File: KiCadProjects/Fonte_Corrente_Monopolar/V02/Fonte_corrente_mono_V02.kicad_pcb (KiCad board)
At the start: 2 copper layers, 90 x 100 mm, 23 parts, among them J1 Vref, J2 tensoes, J3 sinais analogicos, J4 comunicacao / sinais digitais, U1-howland1 AD828AN, U2 INA128, U3-cond1 AD828AN

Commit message: baseado barramento v04
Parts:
- removed SW_kcd1: sw, Chave_Gangorra:chave gangorra 3 pinos
- removed U1-howland1: AD828AN, AD828AN:N_8_ADI
- added J7: Vref, Connector_PinHeader_2.54mm:PinHeader_1x03_P2.54mm_Vertical, F.Cu at (143.6, 42.8)
- added U1: AD828AN, AD828:AD828, F.Cu at (116.2, 118.3)
- J1: value Vref -> alimentacao analogica; footprint Connector_PinHeader_2.54mm:PinHeader_1x03_P2.54mm_Vertical -> Connector_PinHeader_2.54mm:PinHeader_1x08_P2.54mm_Vertical
- J2: value tensoes -> sinais analogicos; footprint Connector_PinSocket_2.54mm:PinSocket_1x08_P2.54mm_Vertical -> Connector_PinHeader_2.54mm:PinHeader_1x27_P2.54mm_Vertical
- J3: value sinais analogicos -> comunicacao / sinais digitais; footprint Connector_PinSocket_2.54mm:PinSocket_1x27_P2.54mm_Vertical -> Connector_PinHeader_2.54mm:PinHeader_1x35_P2.54mm_Vertical
- J4: value comunicacao / sinais digitais -> Change_signal; footprint Connector_PinSocket_2.54mm:PinSocket_1x35_P2.54mm_Vertical -> Connector_PinHeader_2.54mm:PinHeader_1x03_P2.54mm_Vertical
- U2: value INA128 -> INA128-H1
- U3-cond1: footprint AD828AN:N_8_ADI -> AD828:AD828
- moved J4 106.2 mm to (113.7, 134.3), turned to 90 degrees
- moved C4 90.2 mm to (164.7, 44.8)
- moved J3 87.0 mm to (185.8, 45.0)
- moved J1 83.4 mm to (107.1, 45.0), turned to 0 degrees
- moved R11 72.1 mm to (165.1, 57.7), turned to 0 degrees
- moved R12 69.9 mm to (160.4, 57.4), turned to 90 degrees
- moved D2 69.3 mm to (167.6, 71.4)
- moved R10 64.5 mm to (176.1, 51.7), turned to 180 degrees
- moved D1 58.4 mm to (177.9, 64.3)
- moved U3-cond1 56.9 mm to (145.1, 54.7)
- moved C3 48.5 mm to (159.2, 65.5), turned to 0 degrees
- moved R6 44.0 mm to (144.1, 113.5)
- moved R5 41.7 mm to (133.8, 128.6), turned to 0 degrees
- moved R3 35.3 mm to (131.1, 121.9)
- moved U2 34.5 mm to (118.9, 89.2)
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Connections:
- J1 pad 1: +3.3V -> VCC
- J1 pad 2: Net-(D1-K) -> VEE
- J1 pad 3: +5V -> Earth
- J2 pad 1: Earth -> unconnected-(J2-Pin_1-Pad1)
- J2 pad 2: VCC -> unconnected-(J2-Pin_2-Pad2)
- J2 pad 3: VEE -> unconnected-(J2-Pin_3-Pad3)
- J2 pad 4: +9V -> unconnected-(J2-Pin_4-Pad4)
- J2 pad 5: -9V -> unconnected-(J2-Pin_5-Pad5)
- J2 pad 6: +5V -> unconnected-(J2-Pin_6-Pad6)
- J2 pad 7: -5V -> unconnected-(J2-Pin_7-Pad7)
- J2 pad 8: +3.3V -> unconnected-(J2-Pin_8-Pad8)
- J3 pad 1: unconnected-(J3-Pin_1-Pad1) -> +5V
- J3 pad 16: unconnected-(J3-Pin_16-Pad16) -> Earth
- J3 pad 17: unconnected-(J3-Pin_17-Pad17) -> CS1
- J3 pad 18: unconnected-(J3-Pin_18-Pad18) -> CS0
- J3 pad 19: unconnected-(J3-Pin_19-Pad19) -> SPI_clk
- J3 pad 2: unconnected-(J3-Pin_2-Pad2) -> -5V
- J3 pad 20: I1 -> SPI_CIPO
- J3 pad 21: I2 -> SPI_COPI
- J3 pad 22: Ampl1 -> Earth
- J3 pad 23: Ampl2 -> SCL4
- J3 pad 24: Sin1 -> SDA4
- J3 pad 25: Sin2 -> Earth
- J3 pad 26: SinA -> SCL3
- J3 pad 27: SinB -> SDA3
- J3 pad 3: unconnected-(J3-Pin_3-Pad3) -> Earth
- J3 pad 4: unconnected-(J3-Pin_4-Pad4) -> Earth
- J3 pad 5: unconnected-(J3-Pin_5-Pad5) -> +3.3V
- J3 pad 6: unconnected-(J3-Pin_6-Pad6) -> Earth
- J3 pad 7: unconnected-(J3-Pin_7-Pad7) -> Earth
- J4 pad 1: SINC -> SinA
- J4 pad 2: SPI_COPI -> Net-(J4-Pin_2)
- J4 pad 3: SPI_CIPO -> Sin1
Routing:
- net Earth: track 244.0 -> 0.00 mm
- net +3.3V: track 162.9 -> 0.00 mm, vias 2 -> 0
- net +9V: track 151.1 -> 0.00 mm, vias 4 -> 0
- net Net-(U1-howland1-+IN1): track 136.8 -> 0.00 mm
- net -9V: track 126.9 -> 0.00 mm, vias 2 -> 0
- net +5V: track 123.7 -> 0.00 mm
- net out_corrente: track 102.9 -> 0.00 mm, vias 2 -> 0
- net Ampl1: track 74.5 -> 0.00 mm
- net Net-(D1-K): track 63.0 -> 0.00 mm
- net Net-(U1-howland1-+IN2): track 45.4 -> 0.00 mm
- net nó2: track 40.9 -> 0.00 mm
- net SinA: track 31.8 -> 0.00 mm, vias 2 -> 0
- net V_INA: track 24.4 -> 0.00 mm
- net out_buffer: track 23.5 -> 0.00 mm
- net Net-(U1-howland1-OUT2): track 22.5 -> 0.00 mm
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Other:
- board text added: "+3.3V"
- board text added: "+5V"
- board text added: "+9V"
- board text added: "-5V"
- board text added: "-9V"
- board text added: "AGND"
- board text added: "Ampl1"
- board text added: "Ampl2"
- board text added: "CS0"
- board text added: "CS1"
- board text added: "Fonte corrente monopolar V02 2024"
- board text added: "GND"
- board text added: "I1"
- board text added: "I2"
- board text added: "SCL1"
- board text added: "SCL2"
- board text added: "SCL3"
- board text added: "SCL4"
- board text added: "SDA1"
- board text added: "SDA2"
- board text added: "SDA3"
- board text added: "SDA4"
- board text added: "SINCD"
- board text added: "SPI_CIPO"
- board text added: "SPI_COPI"
- board text added: "SPI_clk"
- board text added: "Sin1"
- board text added: "Sin2"
- board text added: "SinA"
- board text added: "SinB"
- board text added: "VCC"
- board text added: "VEE"
- board text removed: "+3.3V | +5.0V"
- board text removed: "Fonte de corrente monopolar Howland aperfeiçoada v01 - 2023"

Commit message: Baseado barramento v04 - Finalizado
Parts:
- SinA | Sin1: renamed from J4
- moved D2 0.38 mm to (167.5, 71.1)
- moved R10 0.38 mm to (176.0, 51.4)
- moved R11 0.38 mm to (164.9, 57.4)
- moved R3 0.38 mm to (130.9, 121.6)
- moved J2 0.38 mm to (106.9, 68.8)
- moved R1 0.38 mm to (126.4, 106.6)
- moved RganhoINA1 0.38 mm to (121.8, 82.6)
- moved SinA | Sin1 0.38 mm to (113.5, 134.0)
- moved U1 0.38 mm to (116.0, 117.9)
- moved U2 0.38 mm to (118.8, 88.9)
- moved R12 0.38 mm to (160.3, 57.1)
- moved U3 0.38 mm to (144.9, 54.3)
- moved R4 0.38 mm to (138.5, 110.0)
- moved R5 0.38 mm to (133.6, 128.3)
- moved J1 0.38 mm to (106.9, 44.7)
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- renumbered U3-cond1 to U3, J7 to Vref
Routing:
- net Earth: track 0.00 -> 335.7 mm
- net +9V: track 0.00 -> 113.2 mm
- net Ampl1: track 0.00 -> 112.7 mm
- net -9V: track 0.00 -> 105.4 mm
- net out_corrente: track 0.00 -> 87.0 mm
- net +3.3V: track 0.00 -> 49.4 mm
- net Net-(D1-K): track 0.00 -> 49.2 mm
- net V_INA: track 0.00 -> 44.0 mm
- net +5V: track 0.00 -> 41.0 mm
- net Net-(U1-howland1-OUT2): track 0.00 -> 23.6 mm
- net Sin1: track 0.00 -> 23.2 mm
- net Net-(U1-howland1--IN2): track 0.00 -> 23.0 mm
- net nó2: track 0.00 -> 20.8 mm
- net I1: track 0.00 -> 18.2 mm
- net Net-(U1-howland1-+IN2): track 0.00 -> 15.1 mm
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- added copper zone on B.Cu, net Earth
- added copper zone on F.Cu, net Earth
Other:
- board text added: "+3.3V | +5.0V"
- board text added: "signal select"

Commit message: Baseado barramento v04 - Finalizado
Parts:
- removed SinA | Sin1: Change_signal, Connector_PinHeader_2.54mm:PinHeader_1x03_P2.54mm_Vertical
- removed U1, U3: AD828AN, AD828:AD828
- removed Vref: Vref, Connector_PinHeader_2.54mm:PinHeader_1x03_P2.54mm_Vertical
- added D3: LED - Red, LED_THT:LED_D5.0mm, F.Cu at (128.0, 44.0)
- added D4: LED - Green, LED_THT:LED_D5.0mm, F.Cu at (121.0, 44.0)
- added D5: LED - Yelow, LED_THT:LED_D5.0mm, F.Cu at (114.0, 44.0)
- added D6: LED - Blue, LED_THT:LED_D5.0mm, F.Cu at (135.0, 44.0)
- added J4: signal select, Connector_PinHeader_2.54mm:PinHeader_1x03_P2.54mm_Vertical, F.Cu at (113.7, 134.0)
- added J7: Vref, Connector_PinHeader_2.54mm:PinHeader_1x03_P2.54mm_Vertical, F.Cu at (149.5, 42.6)
- added R13: 390, Resistor_THT:R_Axial_DIN0207_L6.3mm_D2.5mm_P7.62mm_Horizontal, F.Cu at (122.7, 60.7)
- added R7: 360, Resistor_THT:R_Axial_DIN0207_L6.3mm_D2.5mm_P7.62mm_Horizontal, F.Cu at (119.5, 55.2)
- added R8: 160, Resistor_THT:R_Axial_DIN0207_L6.3mm_D2.5mm_P7.62mm_Horizontal, F.Cu at (143.8, 56.3)
- added R9: 82, Resistor_THT:R_Axial_DIN0207_L6.3mm_D2.5mm_P7.62mm_Horizontal, F.Cu at (136.4, 51.8)
- added U1-howland1: AD828AN, AD828:AD828, F.Cu at (118.7, 113.9)
- added U3-cond1: AD828AN, AD828:AD828, F.Cu at (147.8, 60.1)
- U2: value INA128-H1 -> INA128
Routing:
- net Earth: track 335.7 -> 380.3 mm
- net nó2: track 20.8 -> 50.0 mm
- net Net-(D6-A): track 0.00 -> 19.7 mm
- net out_corrente: track 87.0 -> 67.5 mm
- net Net-(D4-A): track 0.00 -> 18.3 mm
- net Net-(D5-A): track 0.00 -> 15.5 mm
- net +5V: track 41.0 -> 54.3 mm
- net Net-(D3-K): track 0.00 -> 13.0 mm
- net +3.3V: track 49.4 -> 58.9 mm
- net nó1: track 13.5 -> 6.14 mm
- net -9V: track 105.4 -> 112.6 mm
- net Ampl1: track 112.7 -> 107.2 mm
- net out_buffer: track 15.0 -> 9.91 mm
- net Net-(U1-howland1-OUT2): track 23.6 -> 19.0 mm
- net Net-(D1-K): track 49.2 -> 45.0 mm
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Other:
- board text removed: "+3.3V | +5.0V"
- board text removed: "signal select"

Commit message: Baseado barramento v04 - Finalizado - mudanca valor resitor leds
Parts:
- R13: value 390 -> 1.2k
- R7: value 360 -> 1.2k
- R8: value 160 -> 390
- R9: value 82 -> 240
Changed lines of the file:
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@@
         (effects (font (size 1 1) (thickness 0.15)))
     )
-    (fp_text value "82" (at 3.81 2.37) (layer "F.Fab")
+    (fp_text value "240" (at 3.81 2.37) (layer "F.Fab")
         (effects (font (size 1 1) (thickness 0.15)))
     )
@@
         (effects (font (size 1 1) (thickness 0.15)))
     )
-    (fp_text value "160" (at 3.81 2.37) (layer "F.Fab")
+    (fp_text value "390" (at 3.81 2.37) (layer "F.Fab")
         (effects (font (size 1 1) (thickness 0.15)))
     )
@@
         (effects (font (size 1 1) (thickness 0.15)))
     )
-    (fp_text value "360" (at 3.81 2.37) (layer "F.Fab")
+    (fp_text value "1.2k" (at 3.81 2.37) (layer "F.Fab")
         (effects (font (size 1 1) (thickness 0.15)))
     )
@@
         (effects (font (size 1 1) (thickness 0.15)))
     )
-    (fp_text value "390" (at 3.81 2.37) (layer "F.Fab")
-        (effects (font (size 1 1) (thickness 0.15)))
-    )
+    (fp_text value "1.2k" (at 3.81 2.37) (layer "F.Fab")
+        (effects (font (size 1 1) (thickness 0.15)))
+    )

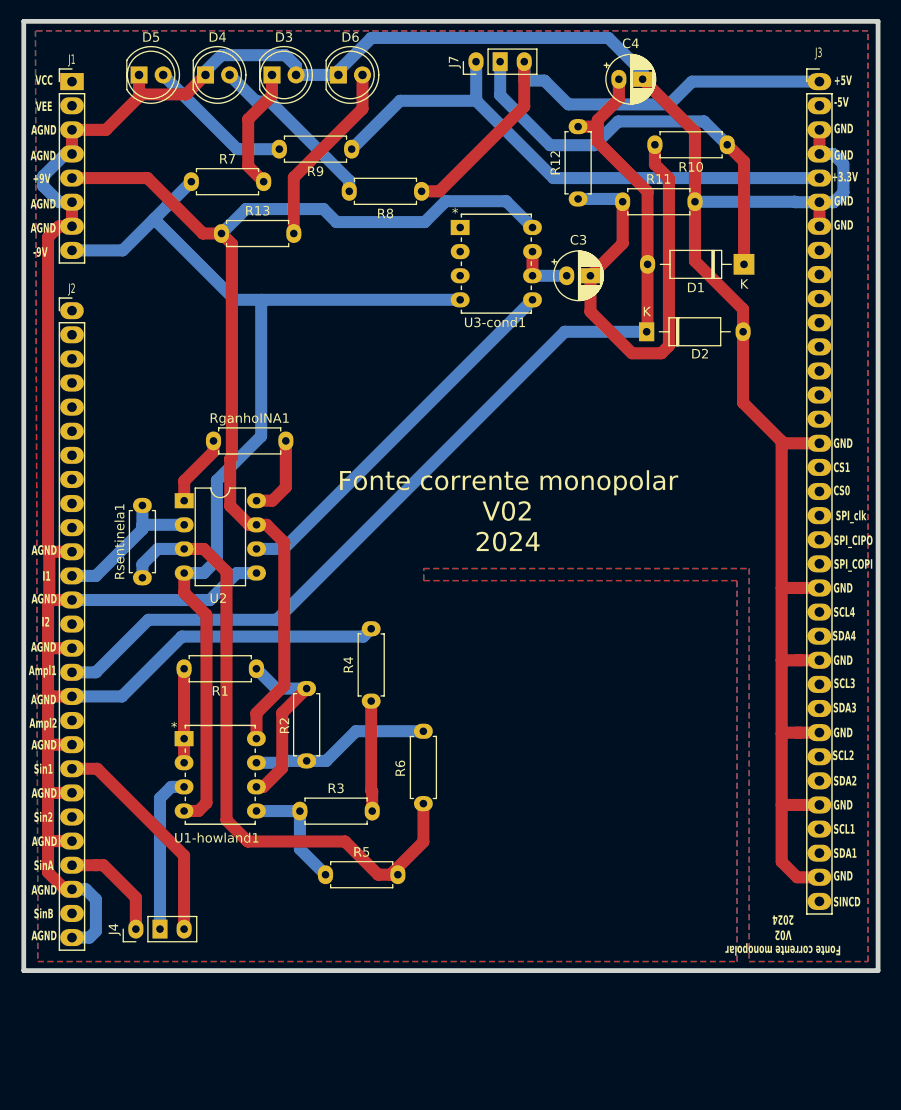
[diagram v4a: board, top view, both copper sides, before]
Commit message: Baseado barramento v04 - Finalizado - mudanca valor resitor leds
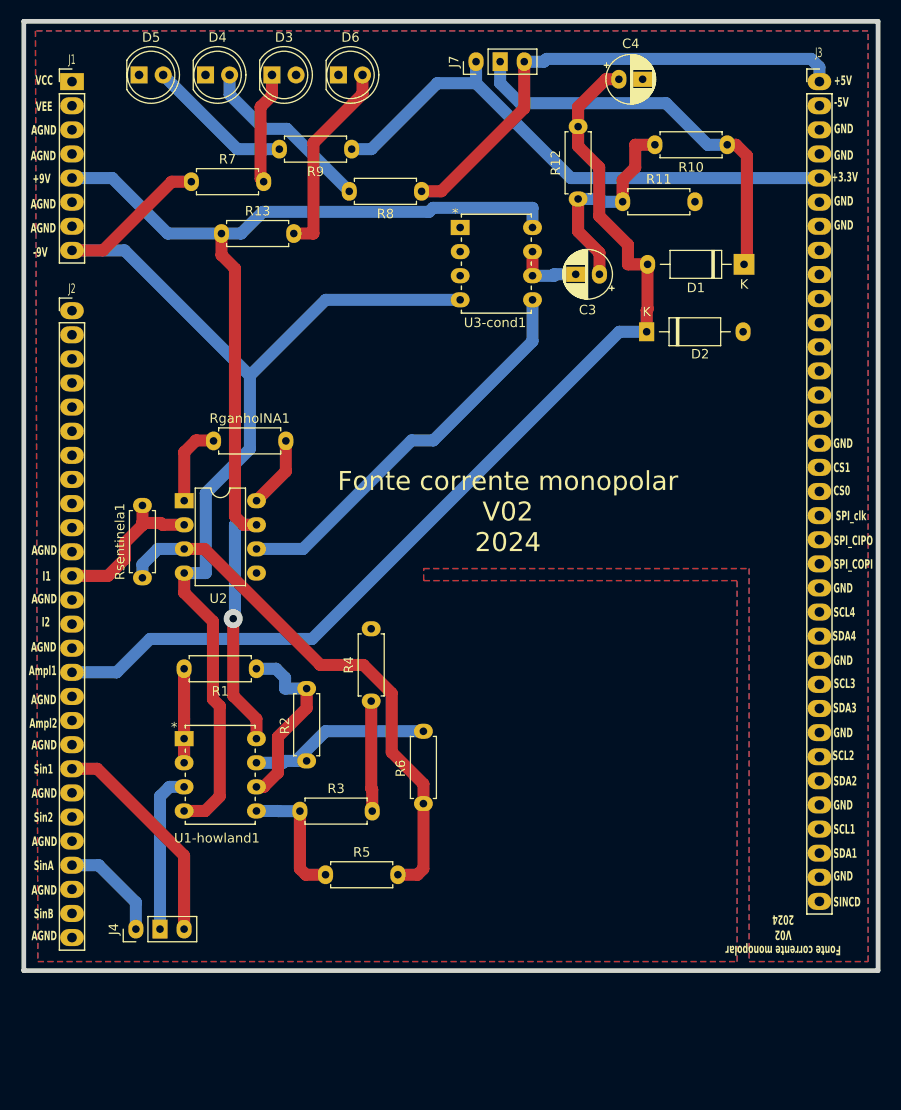
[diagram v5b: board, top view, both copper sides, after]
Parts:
- moved C3 3.45 mm to (162.5, 65.0), turned to 180 degrees
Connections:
- C3 pad 1: nó1 -> nó2
- C3 pad 2: nó2 -> nó1
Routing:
- net Earth: track 380.3 -> 0.00 mm
- net nó2: track 50.0 -> 22.3 mm
- net out_corrente: track 67.5 -> 57.5 mm
- net -9V: track 112.6 -> 119.7 mm
- net V_INA: track 39.9 -> 42.5 mm
- net Net-(D1-K): track 45.0 -> 43.0 mm
- net +5V: track 54.3 -> 52.5 mm
- net Ampl1: track 107.2 -> 108.9 mm
- net Net-(D6-A): track 19.7 -> 20.9 mm
- net Net-(U1-howland1-+IN2): track 12.4 -> 13.6 mm
- net Net-(RganhoINA1-Pad1): track 7.58 -> 8.74 mm
- net Net-(U1-howland1-OUT2): track 19.0 -> 20.1 mm
- net nó1: track 6.14 -> 7.24 mm
- net Net-(D3-K): track 13.0 -> 11.9 mm
- net Net-(RganhoINA1-Pad2): track 8.56 -> 7.58 mm
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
